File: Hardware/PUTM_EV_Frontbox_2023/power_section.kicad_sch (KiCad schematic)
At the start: 12 parts, among them U2 AMS1117-3.3

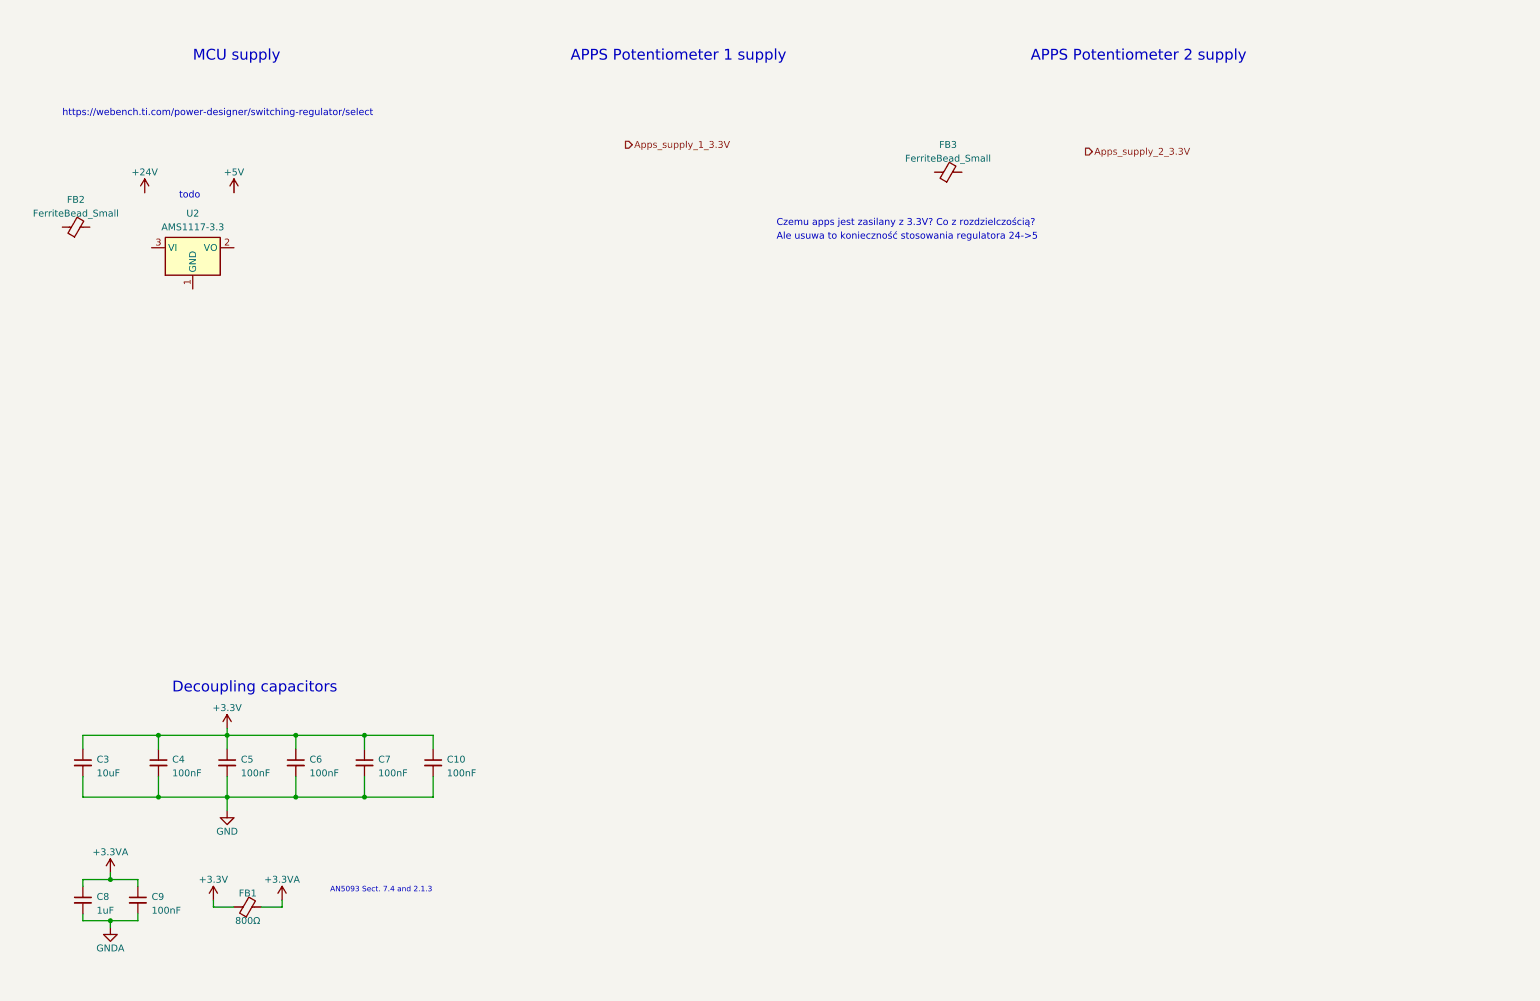
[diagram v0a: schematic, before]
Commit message: Added power section, replaced SWPS
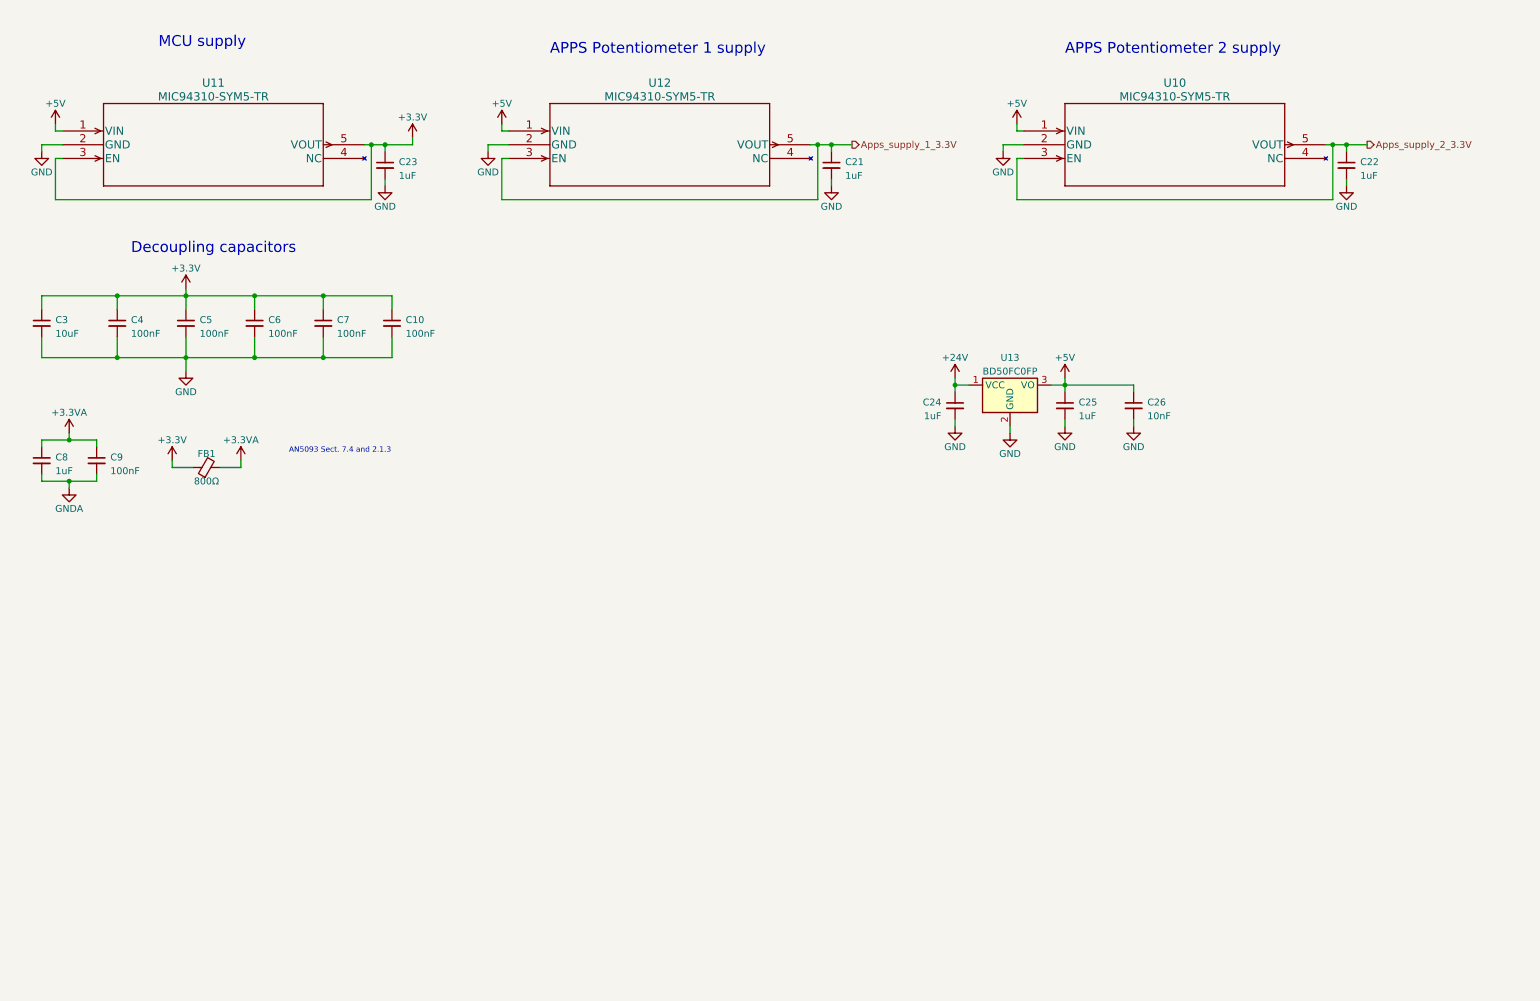
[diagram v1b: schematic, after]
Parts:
- removed FB2, FB3: FerriteBead_Small, symbol Device:FerriteBead_Small
- removed U2: AMS1117-3.3, Package_TO_SOT_SMD:SOT-223-3_TabPin2, symbol Regulator_Linear:AMS1117-3.3
- added C21, C22, C23, C24, C25: 1uF, symbol Device:C_Small
- added C26: 10nF, symbol Device:C_Small
- added U10, U11, U12: MIC94310-SYM5-TR, SOT-23-5_M5_MCH, symbol ul_MIC94310-SYM5-TR:MIC94310-SYM5-TR
- added U13: BD50FC0FP, Package_TO_SOT_SMD:TO-252-2, symbol Regulator_Linear:BD50FC0FP
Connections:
- net +24V: now also C24.1, U13.1 (VCC)
- net +3.3V: now also C23.1, U11.3 (EN), U11.5 (VOUT)
- net +5V: now also C25.1, C26.1, U10.1 (VIN), U11.1 (VIN), U12.1 (VIN), U13.3 (VO)
- net Apps_supply_1_3.3V: now also C21.1, U12.3 (EN), U12.5 (VOUT)
- net Apps_supply_2_3.3V: now also C22.1, U10.3 (EN), U10.5 (VOUT)
- net GND: now also C21.2, C22.2, C23.2, C24.2, C25.2, C26.2, U10.2 (GND), U11.2 (GND), U12.2 (GND), U13.2 (GND)
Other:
- note removed: "Ale usuwa to konieczność stosowania regulatora 24->5"
- note removed: "Czemu apps jest zasilany z 3.3V? Co z rozdzielczością?"
- note removed: "https://webench.ti.com/power-designer/switching-regulator/select"
- note removed: "todo"
- moved on the sheet: C10, C3, C4, C5, C6, C7, C8, C9, FB1

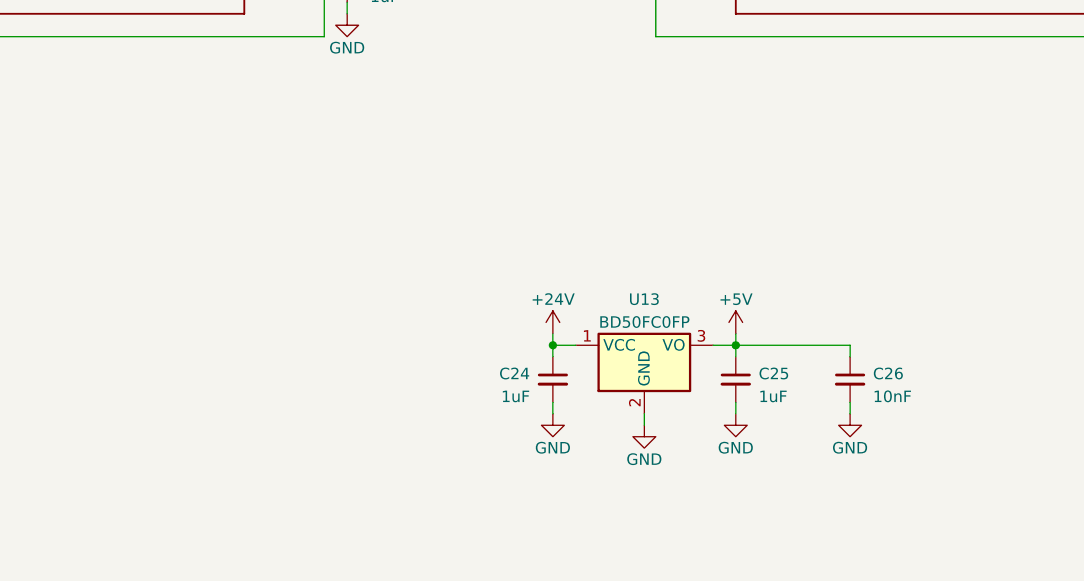
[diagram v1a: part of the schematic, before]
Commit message: Added MCU wiring
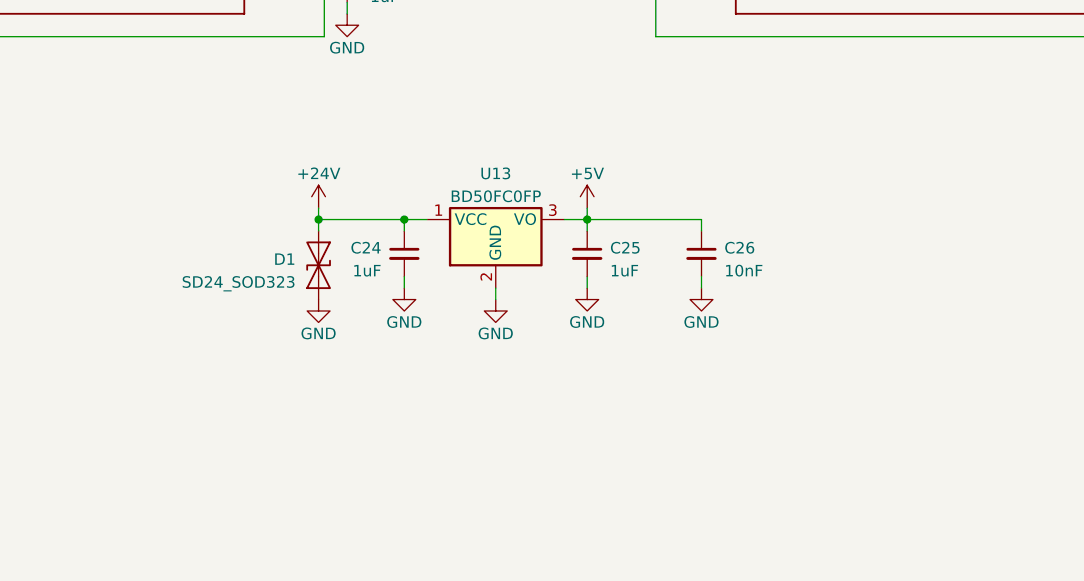
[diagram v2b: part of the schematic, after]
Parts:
- added D1: SD24_SOD323, symbol Diode:SD24_SOD323
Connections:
- net +24V: now also D1.2 (A2)
- net GND: now also D1.1 (A1)
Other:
- moved on the sheet: C24, C25, C26, U13

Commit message: Schematic ready for review
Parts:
- renumbered C6 to C10, C7 to C11, C23 to C12, C10 to C13, C21 to C14, C24 to C15, C25 to C16, C26 to C17, C22 to C18, C3 to C5, C8 to C6, C9 to C7, C4 to C8, C5 to C9, D1 to D6, U11 to U4, U12 to U5, U13 to U6, U10 to U7
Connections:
- net GNDA is gone; now on net GND: C6.2, C7.2
- net Apps_supply_1_3.3V renamed APPS_supply_1_3.3V
- net Apps_supply_2_3.3V renamed APPS_supply_2_3.3V

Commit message: Fixed all issues
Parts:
- removed C5: 10uF, symbol Device:C_Small
- removed U4, U5, U7: MIC94310-SYM5-TR, SOT-23-5_M5_MCH, symbol ul_MIC94310-SYM5-TR:MIC94310-SYM5-TR
- added C36, C37, C38, C43: 1uF, symbol Device:C_Small
- added C39, C47: 10uF, symbol Device:C_Polarized_Small
- added C41, C44: 220nF, symbol Device:C_Small
- added C45: 4u7F, symbol Device:C_Small
- added C46: 100nF, symbol Device:C_Small
- added F1: 1A, symbol Device:Polyfuse_Small
- added F2, F3: 300mA, symbol Device:Polyfuse_Small
- added F4: 1.5A, symbol Device:Fuse_Small
- added L1: 2u2H, symbol Device:L_Small
- added R19: 200R, symbol Device:R_Small
- added R75: 220R, symbol Device:R_Small
- added R87: 100k, symbol Device:R_Small
- added R88: 16k7, symbol Device:R_Small
- added R89: 0R, symbol Device:R_Small
- added U19, U4, U5: TLV743P, symbol Regulator_Linear:TLV73330PDBV
- added U20: LM4040DBZ-5, Package_TO_SOT_SMD:SOT-23, symbol Reference_Voltage:LM4040DBZ-5
- added U7: LM62440-Q1, symbol LMR51420:LM62440
- FB1: value 800Ω -> 1000Ω@100MHz
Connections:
- net +24V: now also F4.1; no longer C15.1, U6.1 (VCC)
- net +3.3V: now also C36.1, C39.1, U19.5 (OUT); no longer C12.1
- net +5V: now also C12.1, C18.1, C37.1, F2.1, F3.1, U19.1 (IN), U19.3 (EN)
- net APPS_supply_1_3.3V: now also R75.2; no longer C14.1
- net APPS_supply_2_3.3V: now also C38.1, U5.5 (OUT); no longer C18.1
- net GND: now also C36.2, C37.2, C38.2, C39.2, C41.2, C43.2, C44.2, C45.2, C47.2, R88.2, U19.2 (GND), U20.2 (A), U4.2 (GND), U5.2 (GND), U7. (VIN2)
- new net: C15.1, F1.2, U6.1 (VCC)
- new net: C41.1, C44.1, C45.1, F4.2, U7. (VIN2)
- new net: F3.2, U5.1 (IN), U5.3 (EN)
- new net: C14.1, R75.1, U4.5 (OUT)
- new net: C46.1, L1.1, U7. (VIN2)
- new net: F2.2, U4.1 (IN), U4.3 (EN)
- new net: C46.2, R89.1, U7. (VIN2)
- new net: C43.1, U7. (VIN2)
- new net: R87.2, R88.1, U7. (VIN2)
- new net: R89.2, U7. (VIN2)
- new net +7.5V: C47.1, F1.1, L1.2, R19.1, R87.1, U7. (VIN2)
- new net 5v_ref: R19.2, U20.1 (K)
- no-connect marks 0 -> 1
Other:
- note added: "Supplies 5V ICs, Suspension potentiometers"
- note added: "This resistor ensures that APPS's potentiometers have non intersecting transfer functions. The other potentiometer has an identical resistor on the negative side."
- moved on the sheet: C10, C11, C13, C15, C16, C17, C6, C7, C8, C9, D6, FB1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

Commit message: Schematic modified, footprints assigned
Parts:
- C10, C11, C12, C13, C14, C15, C16, C17, C18, C36, C37, C38, C41, C43, C44, C46, C6, C7, C8, C9: footprint (none) -> Capacitor_SMD:C_0402_1005Metric_Pad0.74x0.62mm_HandSolder
- C39, C45, C47: footprint (none) -> Capacitor_SMD:CP_Elec_4x5.7
- D6: footprint (none) -> Diode_SMD:D_SOD-323_HandSoldering
- F1, F4: footprint (none) -> Fuse:Fuse_1812_4532Metric_Pad1.30x3.40mm_HandSolder
- F2, F3: footprint (none) -> Fuse:Fuse_0603_1608Metric_Pad1.05x0.95mm_HandSolder
- FB1: footprint (none) -> Inductor_SMD:L_0603_1608Metric
- L1: footprint (none) -> Inductor_SMD:L_Abracon_ASPI-4030S
- R19, R75, R87, R88, R89: footprint (none) -> Resistor_SMD:R_0402_1005Metric
- U19, U4, U5: footprint (none) -> Package_TO_SOT_SMD:SOT-23-5_HandSoldering
- U7: footprint (none) -> Frontbox:IC_LM61460AANRJRR

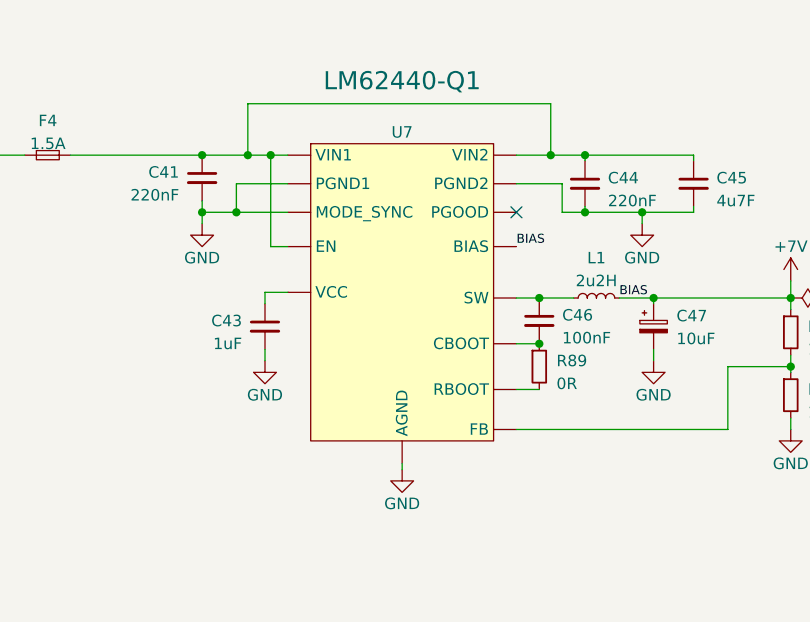
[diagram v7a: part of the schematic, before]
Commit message: Footprints placed, some routing
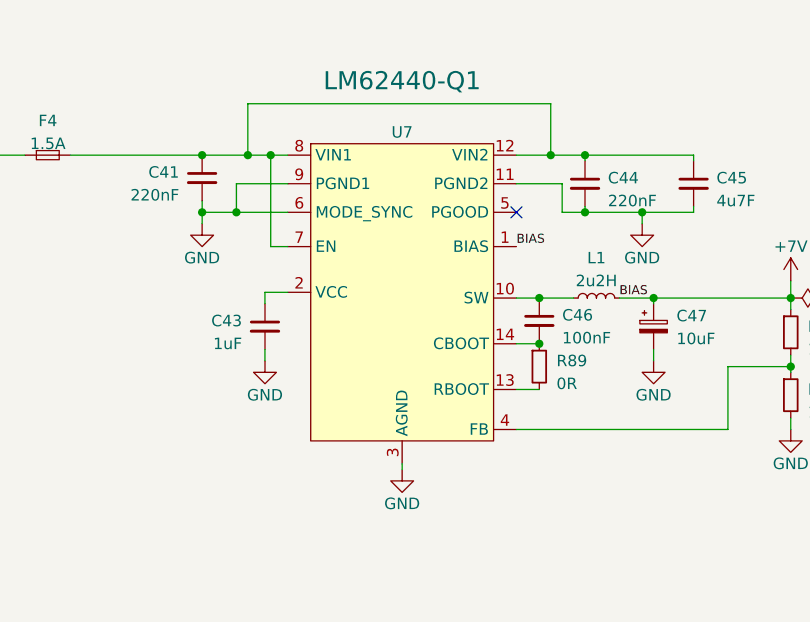
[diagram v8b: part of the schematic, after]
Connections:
- net +7.5V: now also U7.1 (BIAS); no longer U7. (VIN2)
- net GND: now also U7.11 (PGND2), U7.3 (AGND), U7.6 (MODE_SYNC), U7.9 (PGND1); no longer U7. (VIN2)
- net at C41.1, C44.1, C45.1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: now also U7.12 (VIN2), U7.7 (EN), U7.8 (VIN1); no longer U7. (VIN2)
- net at C46.1, L1.1: now also U7.10 (SW); no longer U7. (VIN2)
- net at C46.2, R89.1: now also U7.14 (CBOOT); no longer U7. (VIN2)
- net at C43.1: now also U7.2 (VCC); no longer U7. (VIN2)
- net at R87.2, R88.1: now also U7.4 (FB); no longer U7. (VIN2)
- net at R89.2: now also U7.13 (RBOOT); no longer U7. (VIN2)
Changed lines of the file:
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@@
       (effects (font (size 1.27 1.27)) hide)
     )
-    (pin "")
-    (pin "")
-    (pin "")
-    (pin "")
-    (pin "")
-    (pin "")
-    (pin "")
-    (pin "")
-    (pin "")
-    (pin "")
-    (pin "")
-    (pin "")
-    (pin "")
-    (pin "")
+    (pin "3")
+    (pin "1")
+    (pin "14")
+    (pin "7")
+    (pin "4")
+    (pin "6")
+    (pin "9")
+    (pin "11")
+    (pin "5")
+    (pin "13")
+    (pin "10")
+    (pin "2")
+    (pin "8")
+    (pin "12")
     (instances
       (project "PUTM_EV_Frontbox_2023"
